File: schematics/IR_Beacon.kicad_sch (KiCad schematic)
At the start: 30 parts, among them Q3 LTR3208E, Q4 LTR3208E, U11 MCP6294, U12 MCP6294, U13 LM339AN, U14 LM339AN

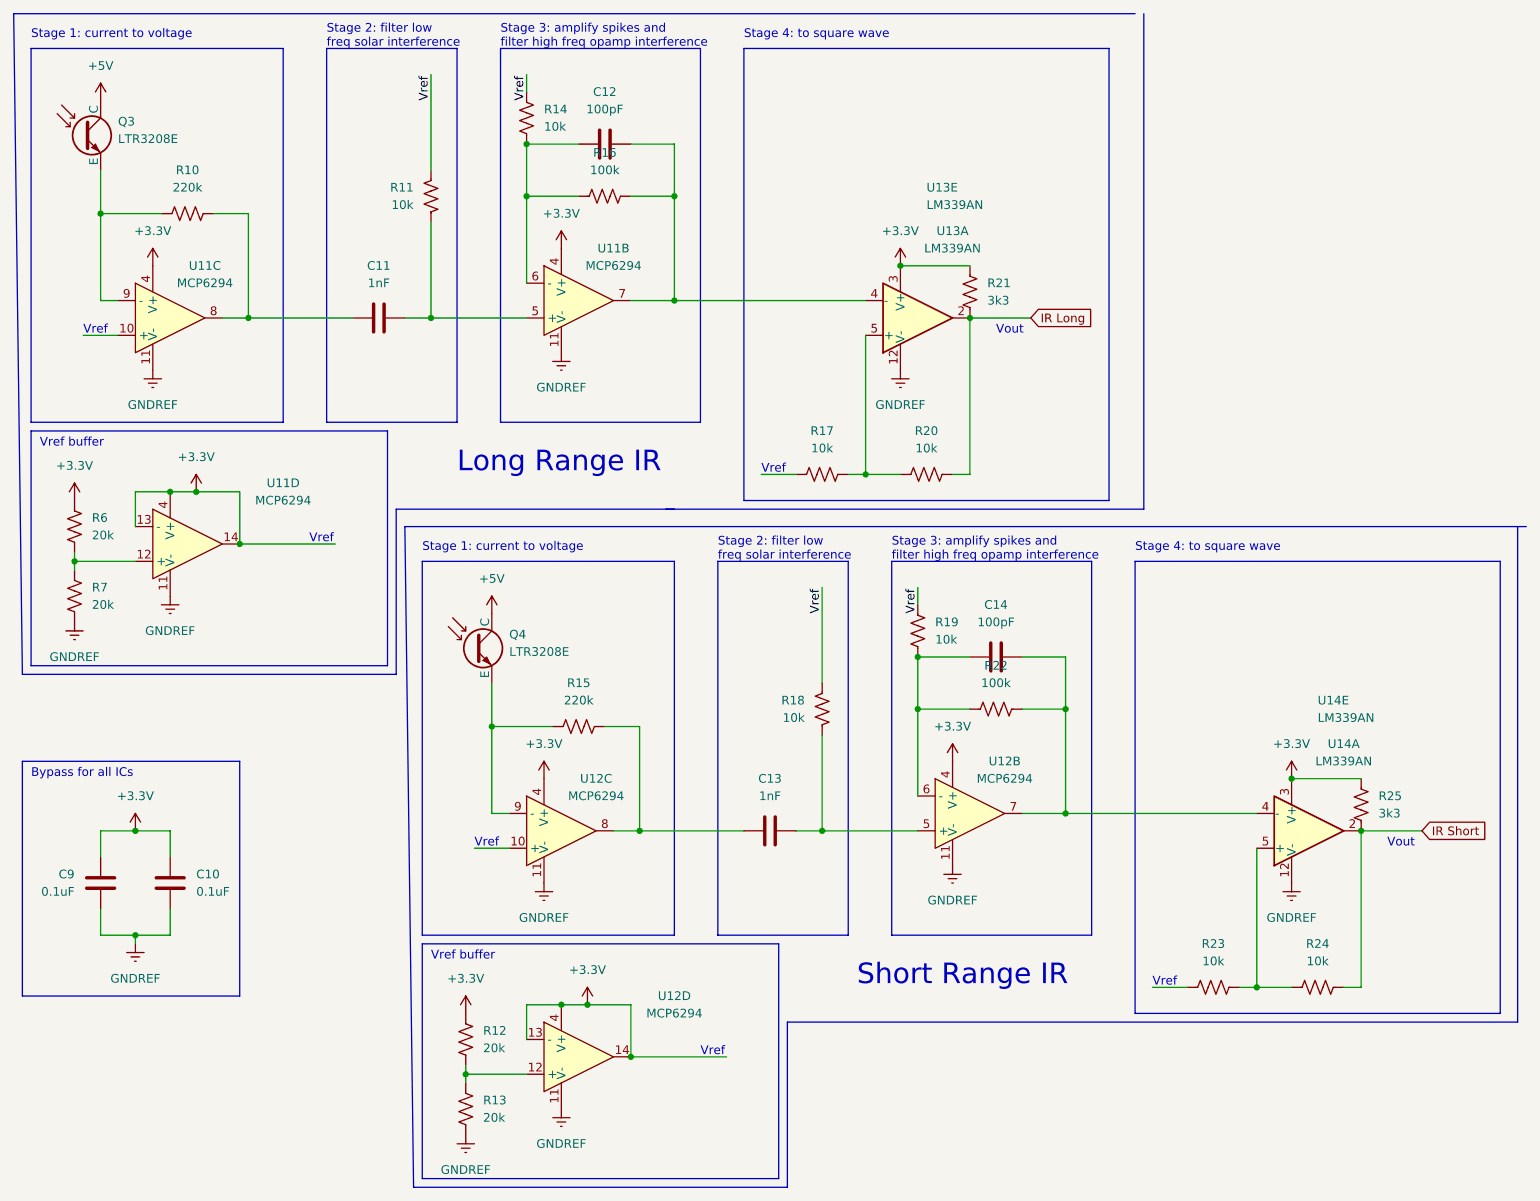
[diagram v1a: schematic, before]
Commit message: Gear SolidWorks files
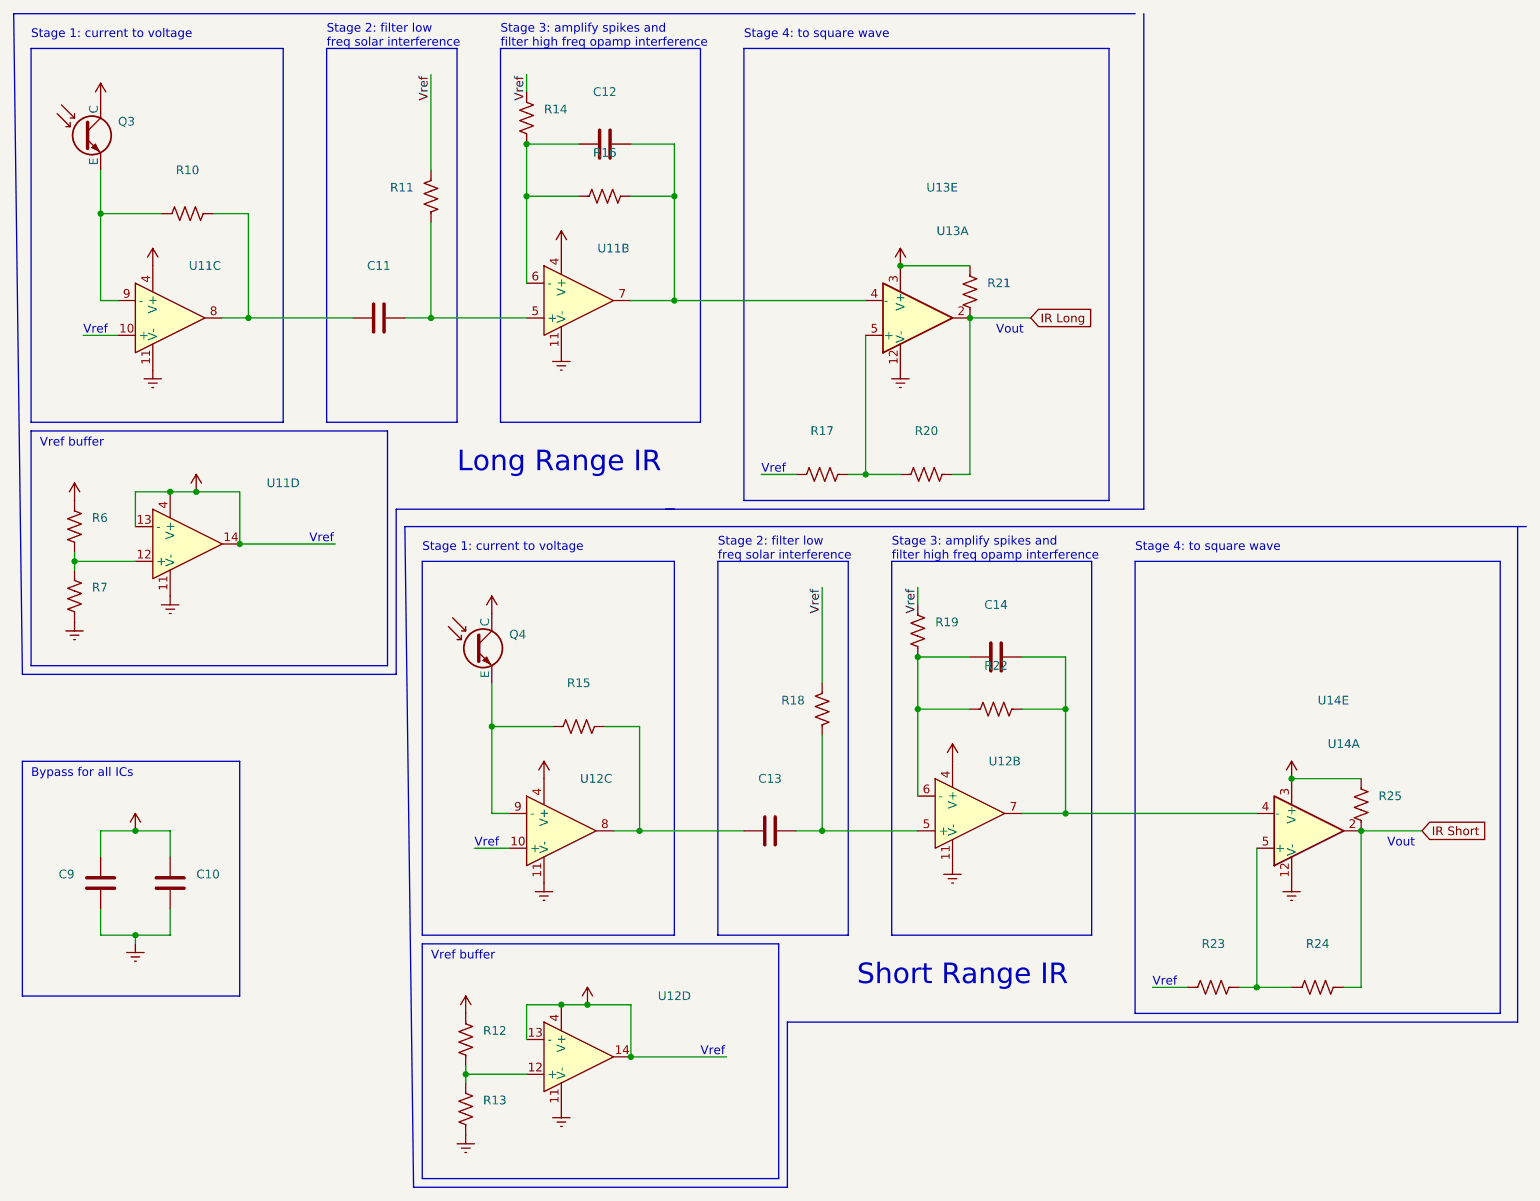
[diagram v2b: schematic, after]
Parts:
- C10, C9: value 0.1uF -> (none)
- C11, C13: value 1nF -> (none)
- C12, C14: value 100pF -> (none)
- Q3, Q4: value LTR3208E -> (none)
- R10, R15: value 220k -> (none)
- R11, R14, R17, R18, R19, R20, R23, R24: value 10k -> (none)
- R12, R13, R6, R7: value 20k -> (none)
- R16, R22: value 100k -> (none)
- R21, R25: value 3k3 -> (none)
- U11, U12: value MCP6294 -> (none)
- U13, U14: value LM339AN -> (none)

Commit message: Choose encoder pins and correct rollover time update.
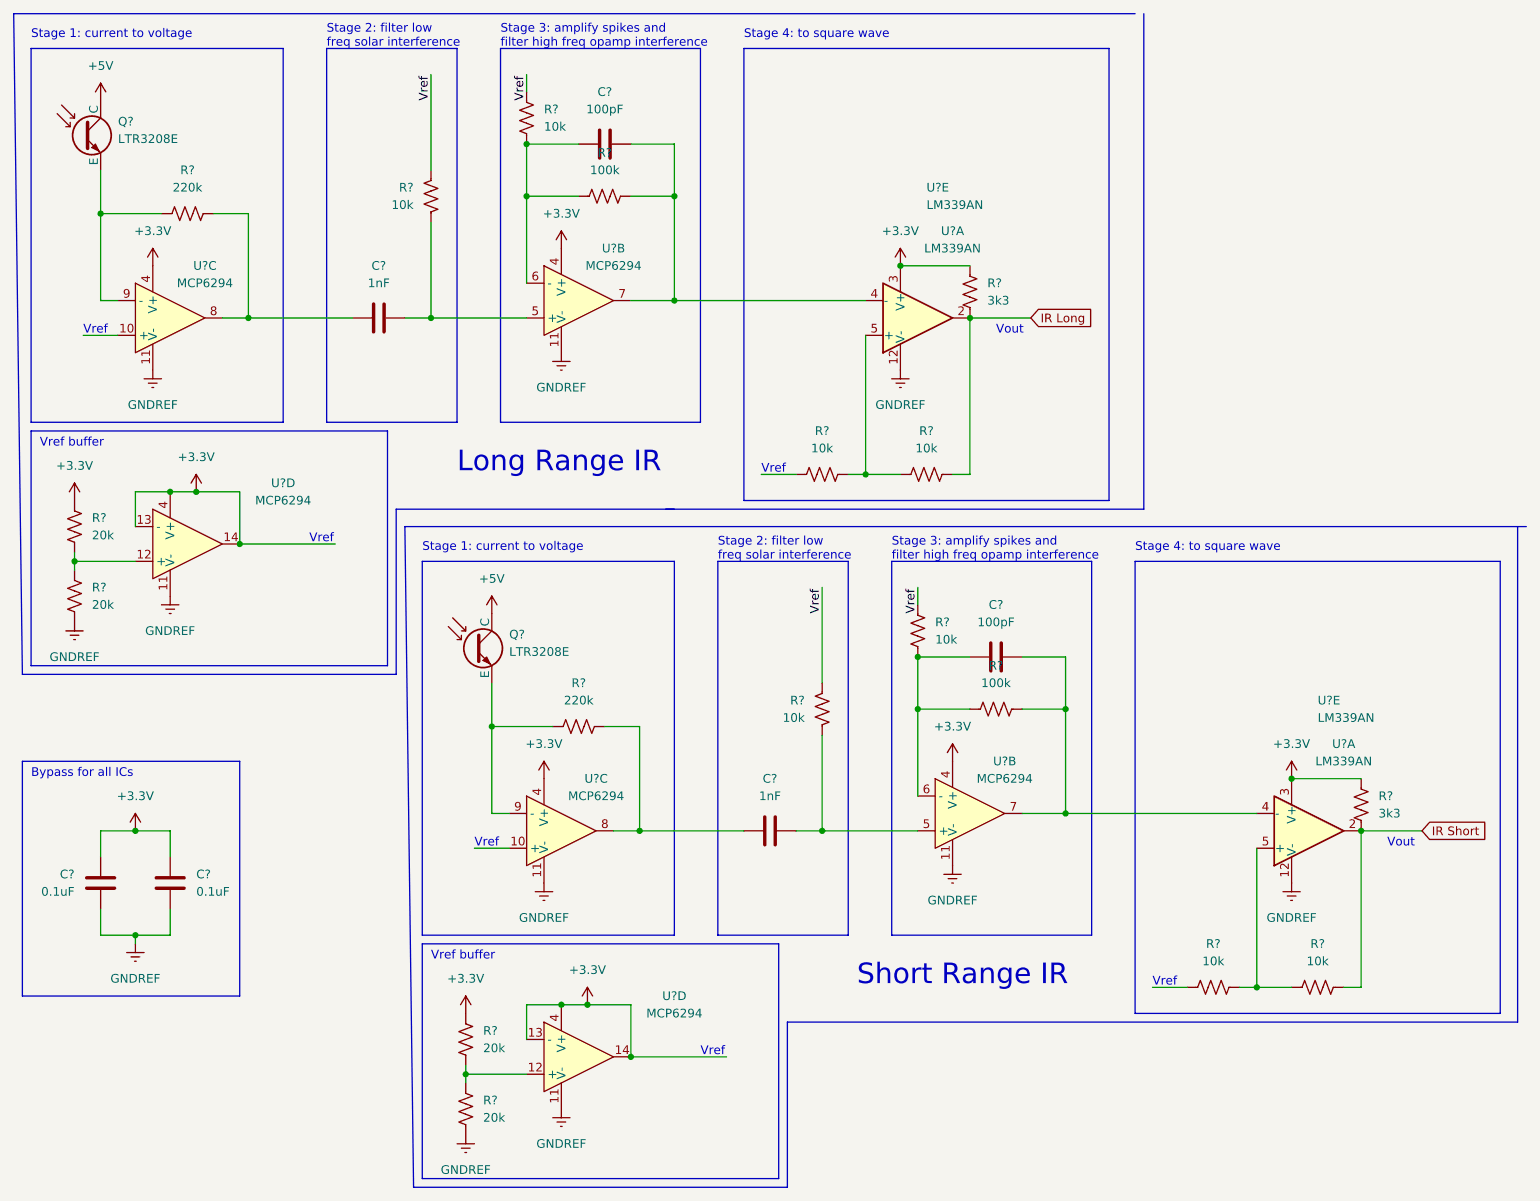
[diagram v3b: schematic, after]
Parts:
- C?: renamed from C13; value (none) -> 1nF
- C?: renamed from C14; value (none) -> 100pF
- C?: renamed from C12; value (none) -> 100pF
- C?: renamed from C9; value (none) -> 0.1uF
- C?: renamed from C10; value (none) -> 0.1uF
- C?: renamed from C11; value (none) -> 1nF
- Q?: renamed from Q3; value (none) -> LTR3208E
- Q?: renamed from Q4; value (none) -> LTR3208E
- R?: renamed from R25; value (none) -> 3k3
- R?: renamed from R14; value (none) -> 10k
- R?: renamed from R12; value (none) -> 20k
- R?: renamed from R17; value (none) -> 10k
- R?: renamed from R21; value (none) -> 3k3
- R?: renamed from R15; value (none) -> 220k
- R?: renamed from R20; value (none) -> 10k
- R?: renamed from R22; value (none) -> 100k
- R?: renamed from R16; value (none) -> 100k
- R?: renamed from R7; value (none) -> 20k
- R?: renamed from R10; value (none) -> 220k
- R?: renamed from R13; value (none) -> 20k
- R?: renamed from R24; value (none) -> 10k
- R?: renamed from R19; value (none) -> 10k
- R?: renamed from R23; value (none) -> 10k
- R?: renamed from R11; value (none) -> 10k
- R?: renamed from R18; value (none) -> 10k
- R?: renamed from R6; value (none) -> 20k
- U? (x2): renamed from U14; value (none) -> LM339AN
- U? (x3): renamed from U11; value (none) -> MCP6294
- U? (x2): renamed from U13; value (none) -> LM339AN
- U? (x3): renamed from U12; value (none) -> MCP6294

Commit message: Update KiCad with new circuits, add screenshots for the website
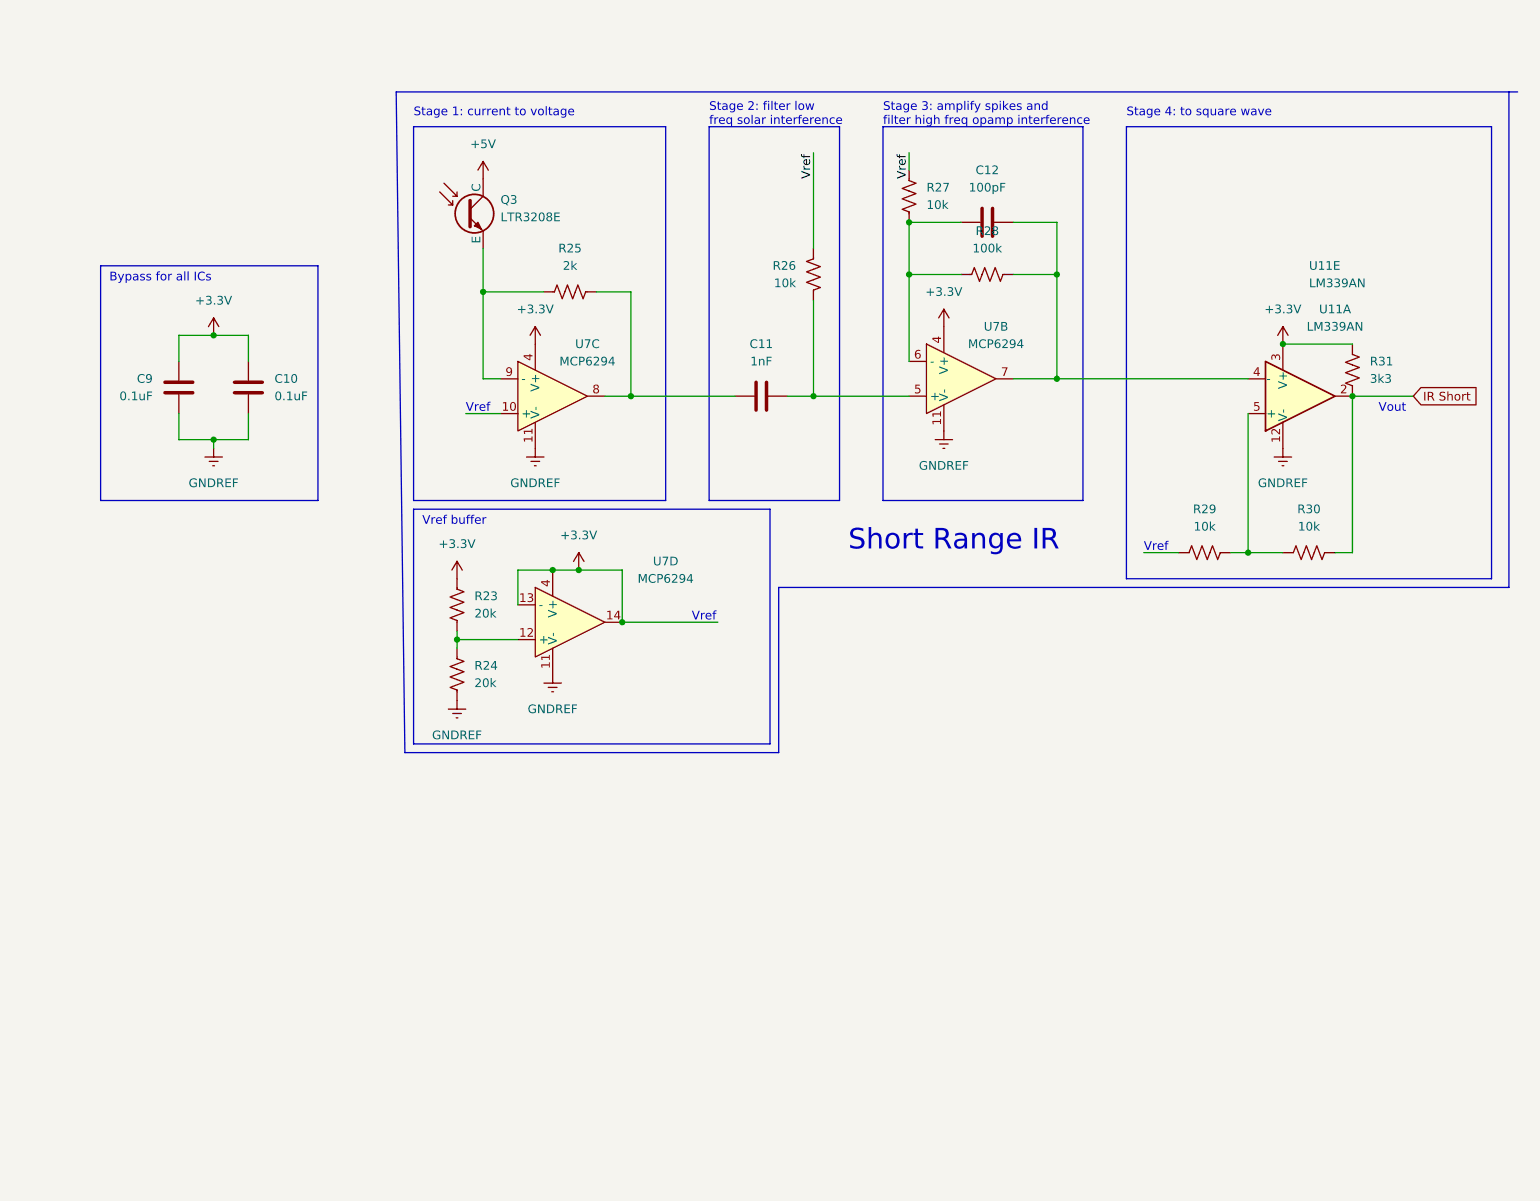
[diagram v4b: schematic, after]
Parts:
- removed C?: 100pF, symbol ME218_BaseLib:Cap
- removed C?: 1nF, symbol ME218_BaseLib:Cap
- removed Q?: LTR3208E, symbol ME218_BaseLib:Photo_NPN
- removed R? (x4): 10k, symbol ME218_BaseLib:Res1
- removed R?: 3k3, symbol ME218_BaseLib:Res1
- removed R?: 100k, symbol ME218_BaseLib:Res1
- removed R? (x2): 20k, symbol ME218_BaseLib:Res1
- removed R?: 220k, symbol ME218_BaseLib:Res1
- removed U? (x3): MCP6294, symbol ME218_BaseLib:MCP6294
- removed U? (x2): LM339AN, symbol ME218_BaseLib:LM339AN
- R25: renamed from R?; value 220k -> 2k
- gave numbers to parts that had none: 15
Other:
- note removed: "Long Range IR"
- moved on the sheet: C10, C11, C12, C9, Q3, R23, R24, R25, R26, R27, R28, R29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
